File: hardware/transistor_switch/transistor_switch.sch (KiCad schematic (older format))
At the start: 6 parts, among them J1 Ard_13_pin, J2 DAC0_arduino, J3 to_biopac, Q1 BC182L_NPN

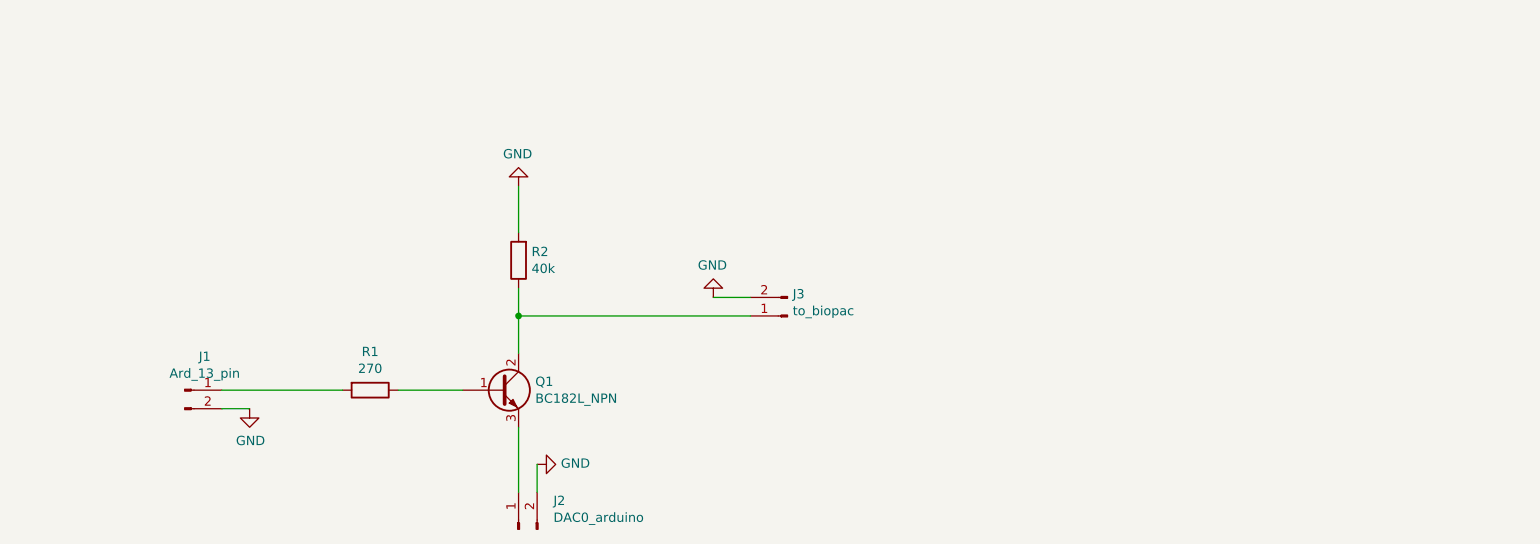
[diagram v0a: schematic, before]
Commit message: updated electronic schematics, exported schematics pdf and made a commented photo of the protoboard
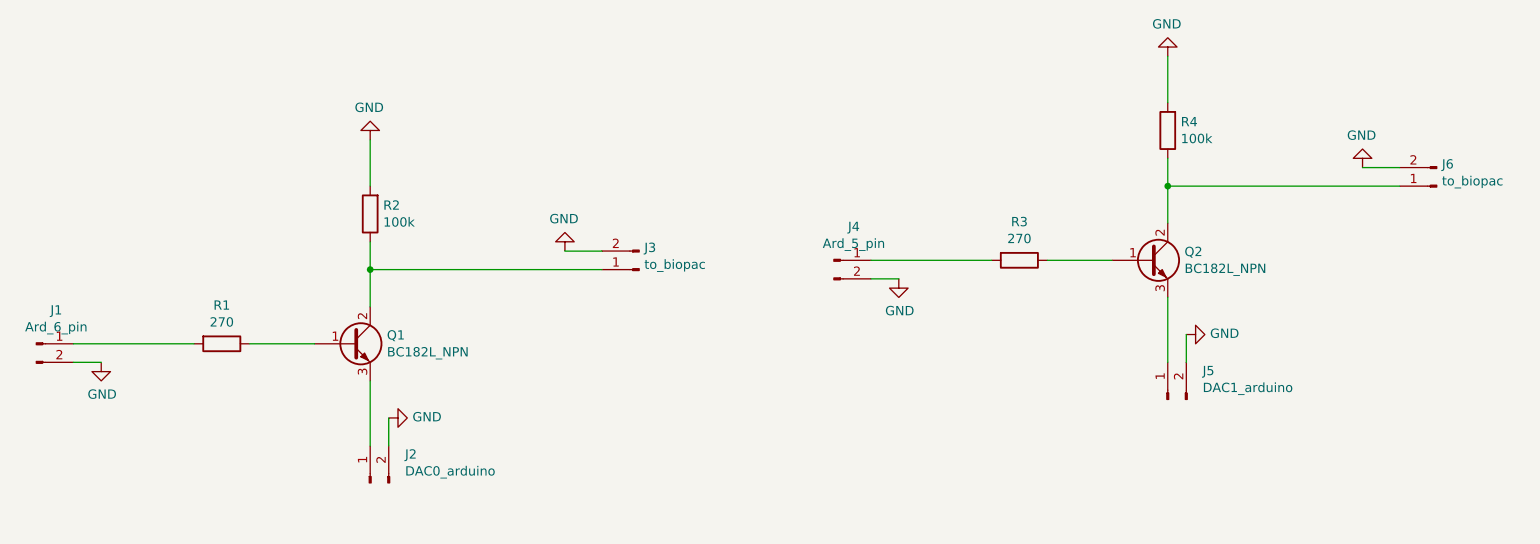
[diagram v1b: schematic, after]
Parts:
- added J4: Ard_5_pin, symbol Connector:Conn_01x02_Male
- added J5: DAC1_arduino, symbol Connector:Conn_01x02_Male
- added J6: to_biopac, symbol Connector:Conn_01x02_Male
- added Q2: BC182L_NPN, symbol Device:Q_NPN_BCE
- added R3: 270, symbol Device:R
- added R4: 100k, symbol Device:R
- J1: value Ard_13_pin -> Ard_6_pin
- R2: value 40k -> 100k
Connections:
- net GND: now also J4.2 (Pin_2), J5.2 (Pin_2), J6.2 (Pin_2), R4.2
- new net: Q2.1 (B), R3.1
- new net: J6.1 (Pin_1), Q2.2 (C), R4.1
- new net: J5.1 (Pin_1), Q2.3 (E)
- new net: J4.1 (Pin_1), R3.2
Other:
- moved on the sheet: J1, J2, J3, Q1, R1, R2
